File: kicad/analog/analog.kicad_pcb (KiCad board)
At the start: 2 copper layers, 75 x 50 mm, 62 parts, among them J301 CONN_02X05, Q201 DMG3414U, Q501 DMG3414U, Q601 DMG3414U, Q701 DMG3414U, U101 NCP694-3.3, U202 LTC2052, U301 SP3003-04, U401 REF5030, U402 LTC2052, U602 LTC2052

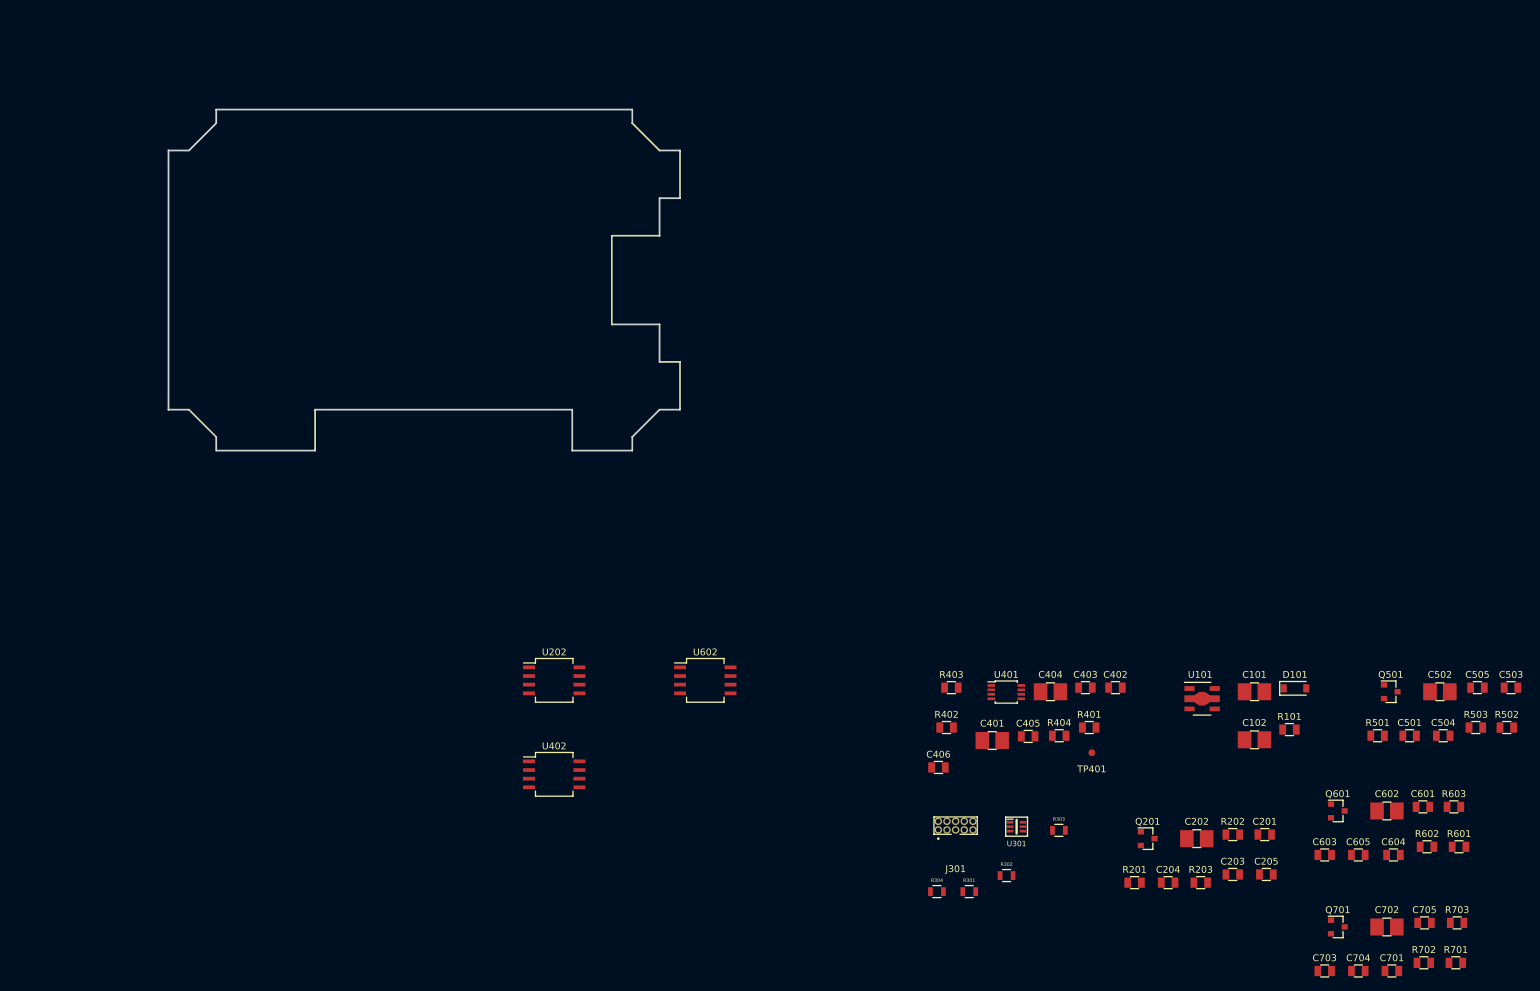
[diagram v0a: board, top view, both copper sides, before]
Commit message: Fix FCI connector refs, footprints, all packages for analog, starting parts placement
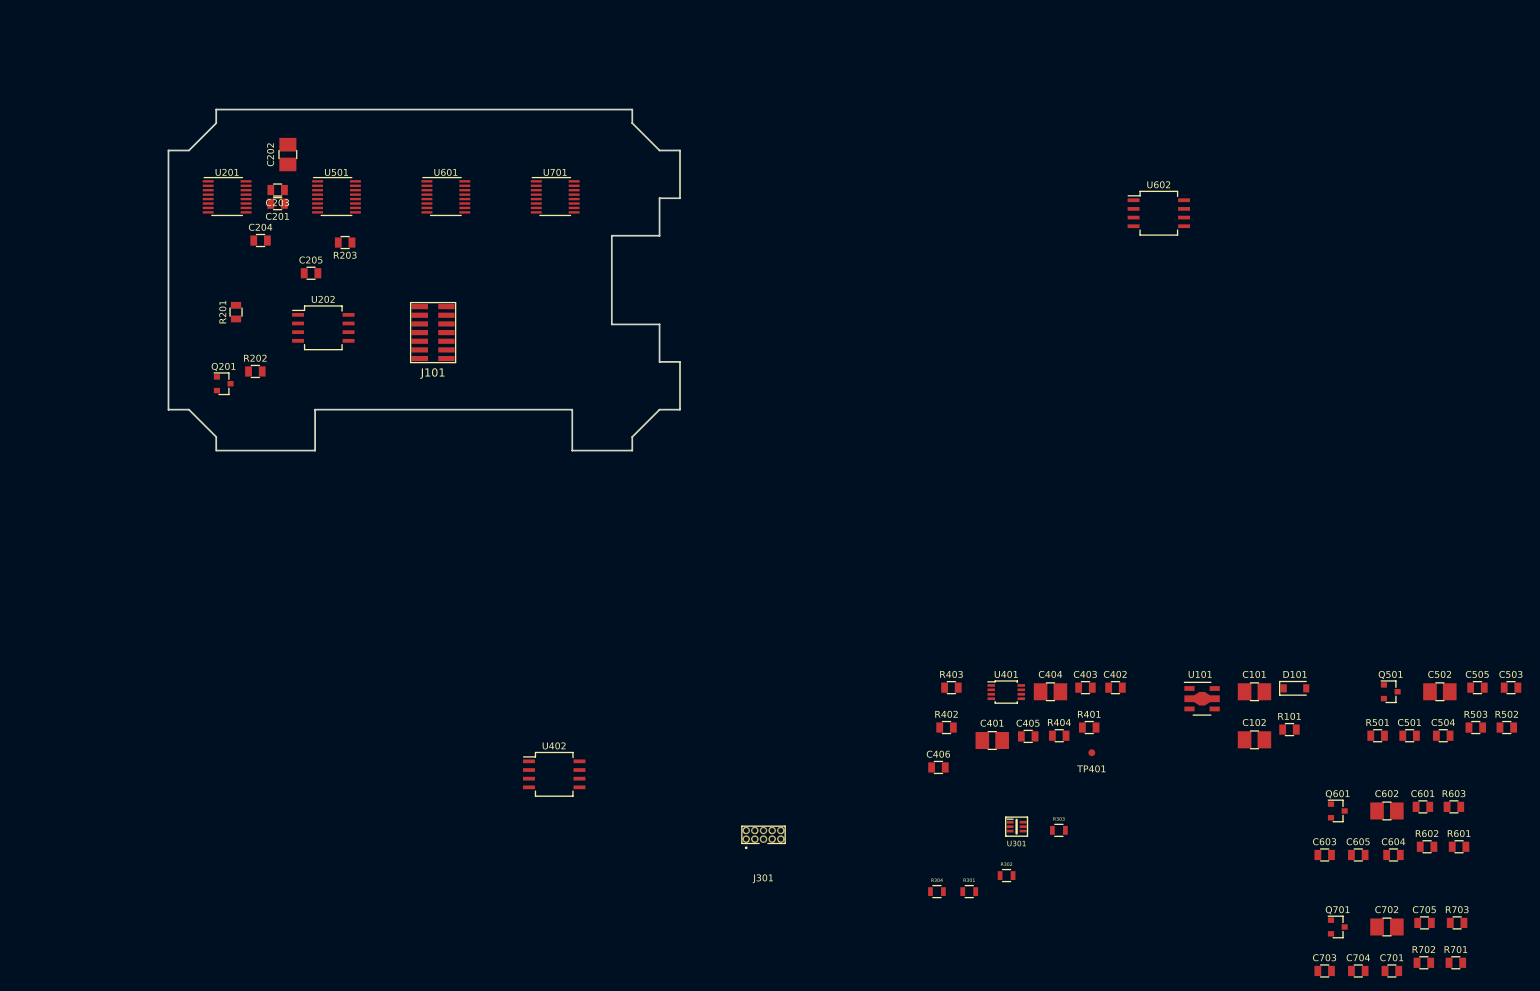
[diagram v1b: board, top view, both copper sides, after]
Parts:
- added J101: FCI 20021221-00014T4LF, paddle:conn_FCI_14_NH, F.Cu at (38.8, 32.7)
- added U201: ADS1220, paddle:TSSOP-16-1EP_4.4x5mm_Pitch0.65mm, F.Cu at (8.60, 12.8)
- added U501: ADS1220, paddle:TSSOP-16-1EP_4.4x5mm_Pitch0.65mm, F.Cu at (24.6, 12.8)
- added U601: ADS1220, paddle:TSSOP-16-1EP_4.4x5mm_Pitch0.65mm, F.Cu at (40.7, 12.8)
- added U701: ADS1220, paddle:TSSOP-16-1EP_4.4x5mm_Pitch0.65mm, F.Cu at (56.7, 12.8)
- moved C203 172.3 mm to (16.0, 11.8), turned to 180 degrees
- moved C201 171.8 mm to (16.0, 13.8), turned to 180 degrees
- moved C202 166.8 mm to (17.5, 6.60), turned to 90 degrees
- moved C205 165.5 mm to (20.9, 24.0)
- moved C204 163.0 mm to (13.5, 19.2)
- moved R202 158.6 mm to (12.7, 38.4)
- moved R203 156.7 mm to (25.9, 19.5), turned to 180 degrees
- moved R201 156.0 mm to (9.90, 29.7), turned to 90 degrees
- moved Q201 151.0 mm to (8.10, 40.2)
- moved U602 95.5 mm to (145.2, 15.2)
- moved U202 61.8 mm to (22.7, 32.0)
- moved J301 28.2 mm to (87.2, 106.3)
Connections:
- U301 pad 5: +3V3 -> +3.3VA
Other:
- copper layers 2 -> 4
- rule pad_to_mask_clearance: 0.2 -> 0.07

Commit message: separate opamps for - input
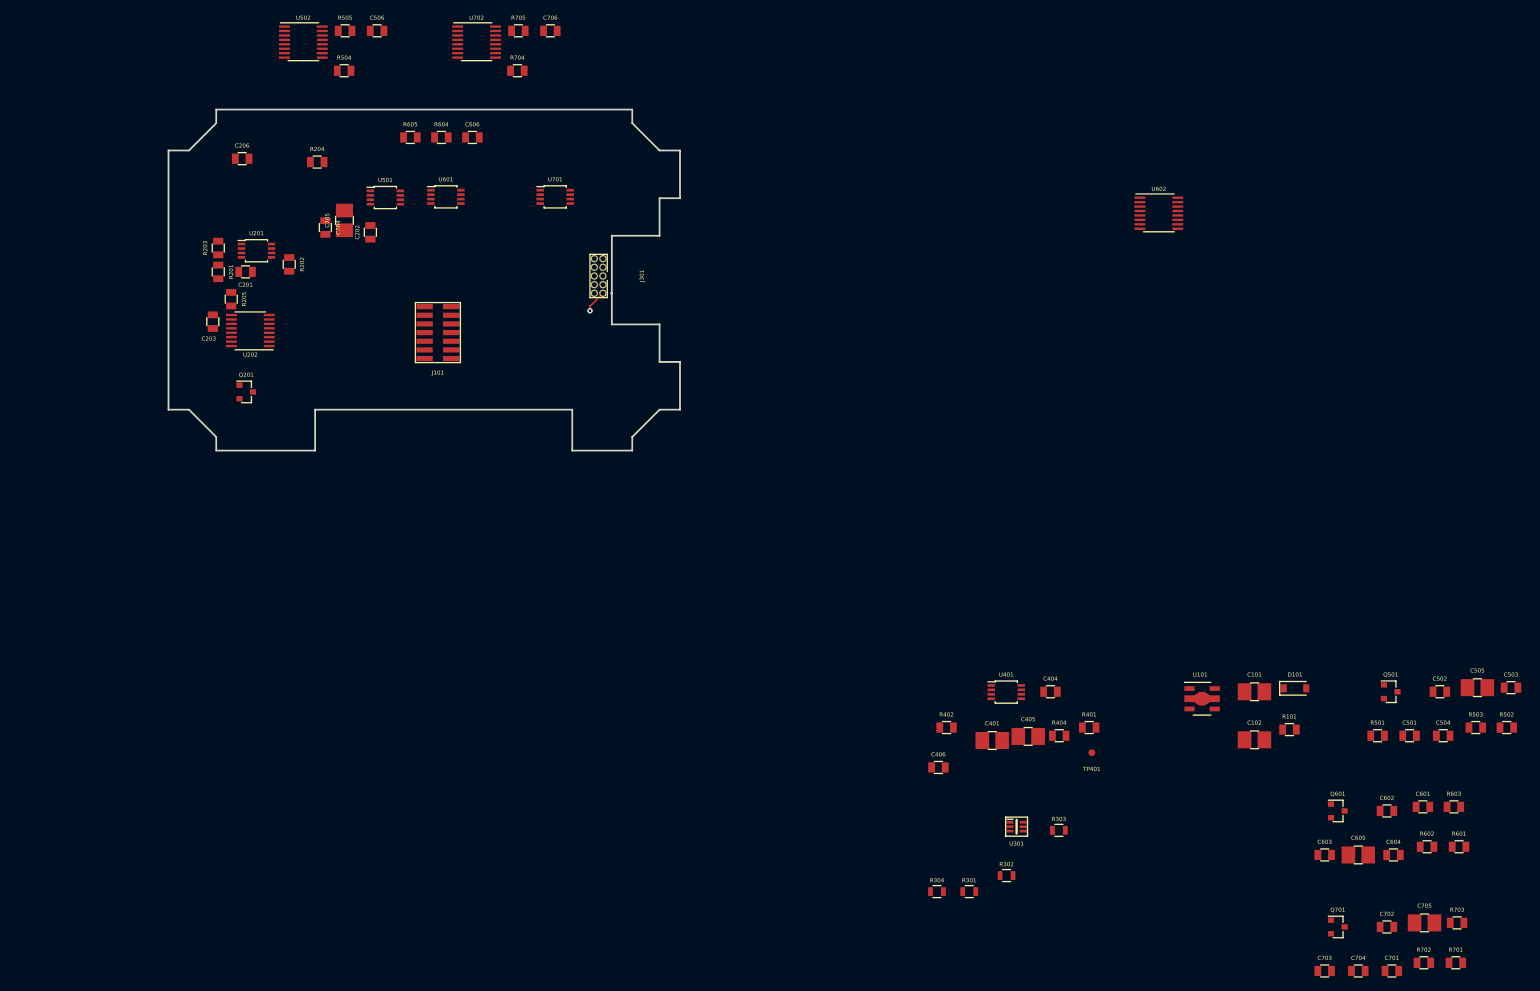
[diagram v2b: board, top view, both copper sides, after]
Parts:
- removed C402, C403: 1uF, paddle:SMD_0805
- removed R403: 20.0k 0.1%, paddle:SMD_0805
- removed U402: LTC2052, paddle:SO-8_5.3x6.2mm_Pitch1.27mm
- added C206: 0.1uF, paddle:SMD_0805, F.Cu at (10.8, 7.20)
- added C506: 0.1uF, paddle:SMD_0805, F.Cu at (30.6, -11.5)
- added C606: 0.1uF, paddle:SMD_0805, F.Cu at (44.6, 4.09)
- added C706: 0.1uF, paddle:SMD_0805, F.Cu at (56.0, -11.5)
- added R204: DNP, paddle:SMD_0805, F.Cu at (21.8, 7.70)
- added R205: 10.0k, paddle:SMD_0805, F.Cu at (9.20, 27.8)
- added R504: DNP, paddle:SMD_0805, F.Cu at (25.8, -5.69)
- added R505: 10.0k, paddle:SMD_0805, F.Cu at (25.9, -11.5)
- added R604: DNP, paddle:SMD_0805, F.Cu at (40.0, 4.09)
- added R605: 10.0k, paddle:SMD_0805, F.Cu at (35.5, 4.09)
- added R704: DNP, paddle:SMD_0805, F.Cu at (51.2, -5.69)
- added R705: 10.0k, paddle:SMD_0805, F.Cu at (51.3, -11.5)
- added U502: ADS1220, paddle:TSSOP-16-1EP_4.4x5mm_Pitch0.65mm, F.Cu at (19.8, -9.89)
- added U702: ADS1220, paddle:TSSOP-16-1EP_4.4x5mm_Pitch0.65mm, F.Cu at (45.2, -9.89)
- C201, C203, C501, C503, C601, C603, C701, C703: value 0.1uF -> 100pF
- C202, C502, C602, C702: value 10uF -> 100pF; footprint paddle:SMD_1206 -> paddle:SMD_0805
- C204, C504, C604, C704: value 100pF -> 0.1uF
- C205, C505, C605, C705: value 100pF -> 10uF; footprint paddle:SMD_0805 -> paddle:SMD_1206
- C404: value 10uF -> 1uF; footprint paddle:SMD_1206 -> paddle:SMD_0805
- C405: value 0.1uF -> 10uF; footprint paddle:SMD_0805 -> paddle:SMD_1206
- C406: value 100pF -> 1uF
- R202, R502, R602, R702: value 10.0k -> 20.0k
- R401: value 1R0 -> 20k 0.1%
- R402: value 20k 0.1% -> 20.0k 0.1%
- R404: value DNP -> 1R0
- U201, U501, U601, U701: value ADS1220 -> LTC2052; footprint paddle:TSSOP-16-1EP_4.4x5mm_Pitch0.65mm -> paddle:TSSOP-8_3x3mm_Pitch0.65mm
- U202, U602: value LTC2052 -> ADS1220; footprint paddle:SO-8_5.3x6.2mm_Pitch1.27mm -> paddle:TSSOP-16-1EP_4.4x5mm_Pitch0.65mm
- moved J301 85.4 mm to (63.1, 24.4), turned to 90 degrees
- moved C203 21.5 mm to (6.50, 31.1), turned to 270 degrees
- moved R203 18.6 mm to (7.30, 20.3), turned to 90 degrees
- moved C202 16.6 mm to (29.6, 18.0)
- moved R202 16.5 mm to (17.7, 22.7), turned to 270 degrees
- moved C201 11.0 mm to (11.3, 23.8)
- moved U202 10.7 mm to (12.0, 32.4), turned to 180 degrees
- moved C204 9.69 mm to (23.0, 17.3), turned to 270 degrees
- moved C205 9.17 mm to (25.8, 16.2), turned to 90 degrees
- moved U201 8.99 mm to (12.9, 20.7)
- moved U501 7.17 mm to (31.8, 12.9)
- moved R201 6.45 mm to (7.30, 23.8), turned to 270 degrees
- moved Q201 3.51 mm to (11.4, 41.4)
- moved J101 0.70 mm to (39.5, 32.7)
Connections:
- C201 pad 2: +3.3VA -> Net-(C201-Pad2)
- C202 pad 1: +3.3VA -> GND
- C202 pad 2: GND -> Net-(C202-Pad2)
- C203 pad 1: GND -> Net-(C203-Pad1)
- C203 pad 2: +3.3VA -> GND
- C204 pad 1: Net-(C204-Pad1) -> GND
- C204 pad 2: GND -> +3.3VA
- C205 pad 1: GND -> +3.3VA
- C205 pad 2: Net-(C205-Pad2) -> GND
- C405 pad 1: GND -> Net-(C405-Pad1)
- C405 pad 2: +3.3VA -> GND
- C406 pad 1: GND -> /VREF
- C406 pad 2: Net-(C406-Pad2) -> GND
- C501 pad 2: +3.3VA -> Net-(C501-Pad2)
- C502 pad 1: +3.3VA -> GND
- C502 pad 2: GND -> Net-(C502-Pad2)
- C503 pad 1: GND -> Net-(C503-Pad1)
- C503 pad 2: +3.3VA -> GND
- C504 pad 1: Net-(C504-Pad1) -> GND
- C504 pad 2: GND -> +3.3VA
- C505 pad 1: GND -> +3.3VA
- C505 pad 2: Net-(C505-Pad2) -> GND
- C601 pad 2: +3.3VA -> Net-(C601-Pad2)
- C602 pad 1: +3.3VA -> GND
- C602 pad 2: GND -> Net-(C602-Pad2)
- C603 pad 1: GND -> Net-(C603-Pad1)
- C603 pad 2: +3.3VA -> GND
- C604 pad 1: Net-(C604-Pad1) -> GND
- C604 pad 2: GND -> +3.3VA
- C605 pad 1: GND -> +3.3VA
- C605 pad 2: Net-(C605-Pad2) -> GND
- C701 pad 2: +3.3VA -> Net-(C701-Pad2)
- C702 pad 1: +3.3VA -> GND
- C702 pad 2: GND -> Net-(C702-Pad2)
- C703 pad 1: GND -> Net-(C703-Pad1)
- C703 pad 2: +3.3VA -> GND
- C704 pad 1: Net-(C704-Pad1) -> GND
- C704 pad 2: GND -> +3.3VA
- C705 pad 1: GND -> +3.3VA
- C705 pad 2: Net-(C705-Pad2) -> GND
- R201 pad 1: +3.3VA -> Net-(C201-Pad2)
- R201 pad 2: Net-(C204-Pad1) -> /IN_
- R202 pad 1: Net-(C205-Pad2) -> Net-(C202-Pad2)
- R202 pad 2: /IN_ -> /BRIDGE_COMP
- R203 pad 1: Net-(C205-Pad2) -> Net-(C201-Pad2)
- R401 pad 1: Net-(C404-Pad1) -> /BRIDGE_COMP
- R401 pad 2: /VREF -> +3.3VA
- R402 pad 1: Net-(C406-Pad2) -> GND
- R402 pad 2: +3.3VA -> /BRIDGE_COMP
- R404 pad 1: Net-(C406-Pad2) -> Net-(C405-Pad1)
- R404 pad 2: /BRIDGE_COMP -> /VREF
- R501 pad 1: +3.3VA -> Net-(C501-Pad2)
- R501 pad 2: Net-(C504-Pad1) -> /IN_
- R502 pad 1: Net-(C505-Pad2) -> Net-(C502-Pad2)
- R502 pad 2: /IN_ -> /BRIDGE_COMP
- R503 pad 1: Net-(C505-Pad2) -> Net-(C501-Pad2)
- R601 pad 1: +3.3VA -> Net-(C601-Pad2)
- R601 pad 2: Net-(C604-Pad1) -> /IN_
- R602 pad 1: Net-(C605-Pad2) -> Net-(C602-Pad2)
- R602 pad 2: /IN_ -> /BRIDGE_COMP
- R603 pad 1: Net-(C605-Pad2) -> Net-(C601-Pad2)
- R701 pad 1: +3.3VA -> Net-(C701-Pad2)
- R701 pad 2: Net-(C704-Pad1) -> /IN_
- R702 pad 1: Net-(C705-Pad2) -> Net-(C702-Pad2)
- R702 pad 2: /IN_ -> /BRIDGE_COMP
- R703 pad 1: Net-(C705-Pad2) -> Net-(C701-Pad2)
- U201 pad 1: /SPI_SCLK -> Net-(R203-Pad2)
- U201 pad 2: /AN0_CS* -> Net-(R203-Pad2)
- U201 pad 3: GND -> Net-(C201-Pad2)
- U201 pad 5: GND -> Net-(C202-Pad2)
- U201 pad 6: GND -> Net-(R204-Pad2)
- U201 pad 7: /BRIDGE_COMP -> Net-(R204-Pad2)
- U201 pad 8: GND -> +3.3VA
- U202 pad 1: Net-(R203-Pad2) -> /SPI_SCLK
- U202 pad 2: Net-(R203-Pad2) -> /AN0_CS*
- U202 pad 3: Net-(C205-Pad2) -> GND
- U202 pad 5: Net-(C505-Pad2) -> GND
- U202 pad 6: Net-(R503-Pad2) -> GND
- U202 pad 7: Net-(R503-Pad2) -> Net-(R204-Pad2)
- U202 pad 8: +3.3VA -> GND
- U401 pad 5: Net-(C403-Pad1) -> Net-(C404-Pad1)
- U501 pad 1: /SPI_SCLK -> Net-(R503-Pad2)
- U501 pad 2: /AN1_CS* -> Net-(R503-Pad2)
- U501 pad 3: GND -> Net-(C501-Pad2)
- U501 pad 5: GND -> Net-(C502-Pad2)
- U501 pad 6: GND -> Net-(R504-Pad2)
- U501 pad 7: /BRIDGE_COMP -> Net-(R504-Pad2)
- U501 pad 8: GND -> +3.3VA
- U601 pad 1: /SPI_SCLK -> Net-(R603-Pad2)
- U601 pad 2: /AN2_CS* -> Net-(R603-Pad2)
- U601 pad 3: GND -> Net-(C601-Pad2)
- U601 pad 5: GND -> Net-(C602-Pad2)
- U601 pad 6: GND -> Net-(R604-Pad2)
- U601 pad 7: /BRIDGE_COMP -> Net-(R604-Pad2)
- U601 pad 8: GND -> +3.3VA
- U602 pad 1: Net-(R603-Pad2) -> /SPI_SCLK
- U602 pad 2: Net-(R603-Pad2) -> /AN2_CS*
- U602 pad 3: Net-(C605-Pad2) -> GND
- U602 pad 5: Net-(C705-Pad2) -> GND
- U602 pad 6: Net-(R703-Pad2) -> GND
- U602 pad 7: Net-(R703-Pad2) -> Net-(R604-Pad2)
- U602 pad 8: +3.3VA -> GND
- U701 pad 1: /SPI_SCLK -> Net-(R703-Pad2)
- U701 pad 2: /AN3_CS* -> Net-(R703-Pad2)
- U701 pad 3: GND -> Net-(C701-Pad2)
- U701 pad 5: GND -> Net-(C702-Pad2)
- U701 pad 6: GND -> Net-(R704-Pad2)
- U701 pad 7: /BRIDGE_COMP -> Net-(R704-Pad2)
- U701 pad 8: GND -> +3.3VA
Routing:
- net +3.3VA: track 0.00 -> 3.91 mm, vias 0 -> 1
- added copper zone on In2.Cu, net +3.3VA
- added copper zone on In1.Cu, net GND

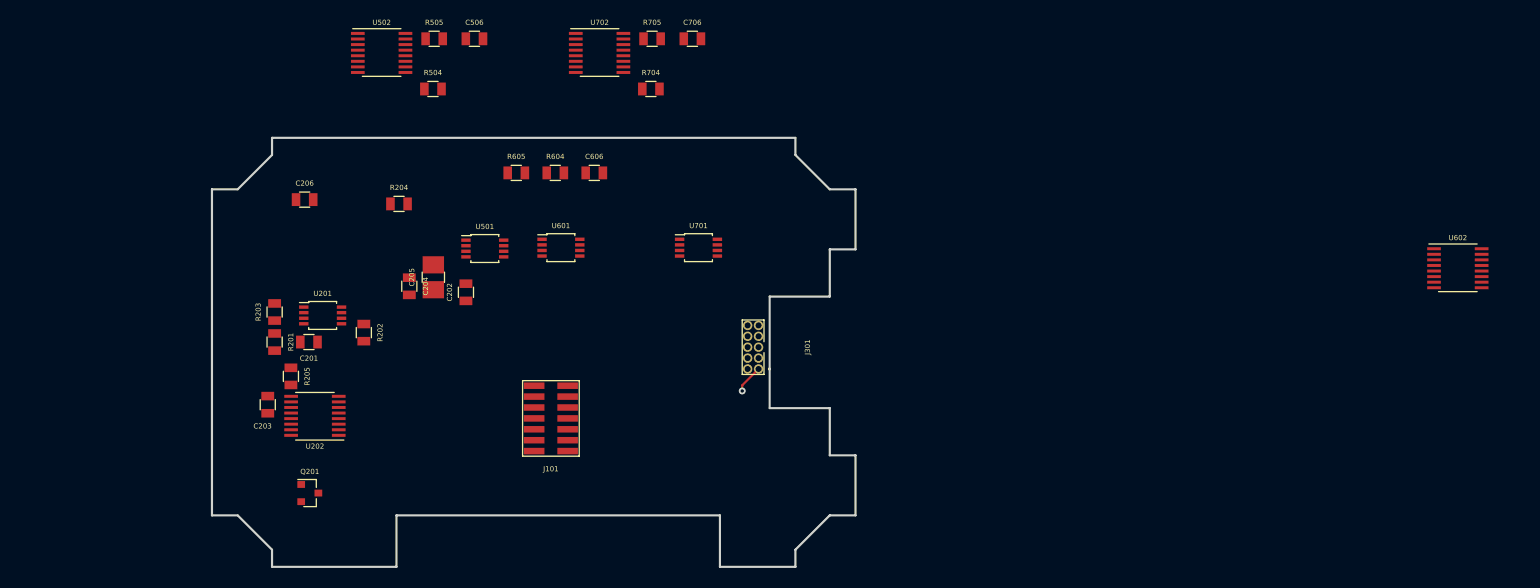
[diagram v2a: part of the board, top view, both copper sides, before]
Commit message: Sch: Added bypass caps opamps
Layout: placement and traces for 1 a/d channel ok, connector in right location and pinout (mirror image of processor)
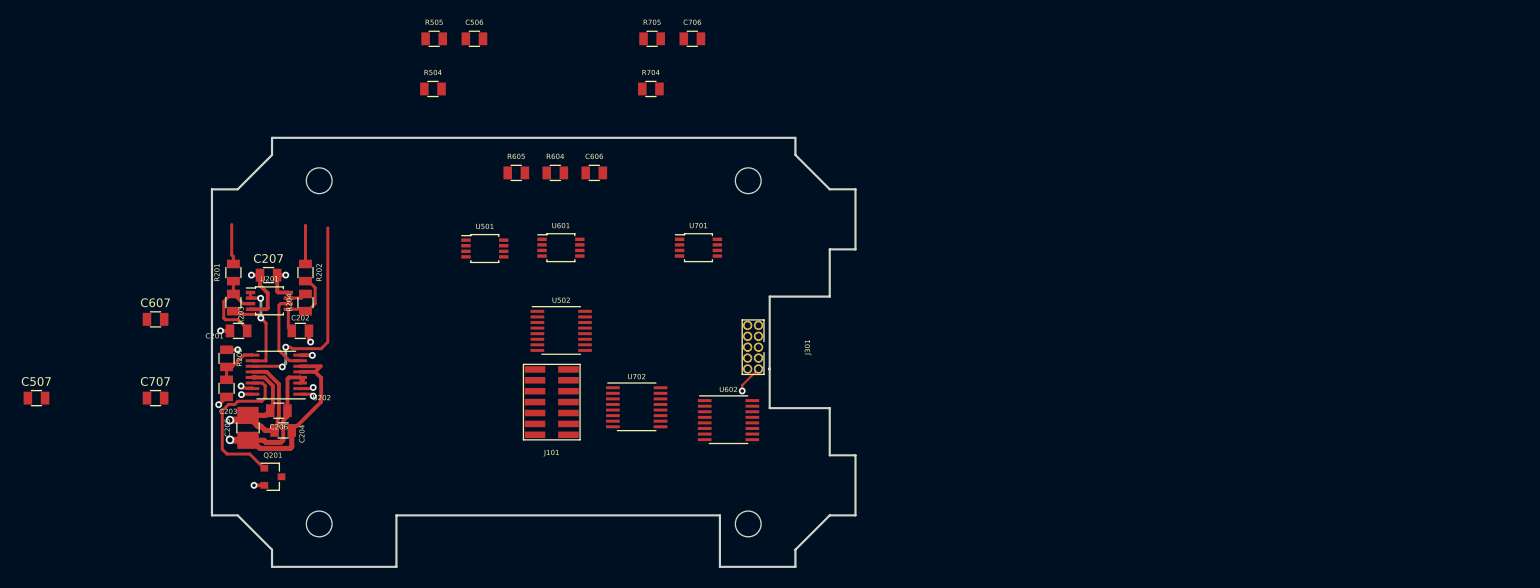
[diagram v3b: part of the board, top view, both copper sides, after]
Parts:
- added C207: 0.1uF, paddle:SMD_0805, F.Cu at (6.60, 16.0)
- added C507: 0.1uF, paddle:SMD_0805, F.Cu at (-20.5, 30.3)
- added C607: 0.1uF, paddle:SMD_0805, F.Cu at (-6.57, 21.2)
- added C707: 0.1uF, paddle:SMD_0805, F.Cu at (-6.57, 30.3)
- added REF**: hole, paddle:KH_F20_mounting_hole, F.Cu at (12.5, 45.0)
- added REF**: hole, paddle:KH_F20_mounting_hole, F.Cu at (62.5, 45.0)
- added REF**: hole, paddle:KH_F20_mounting_hole, F.Cu at (62.5, 5.00)
- added REF**: hole, paddle:KH_F20_mounting_hole, F.Cu at (12.5, 5.00)
- moved U602 86.8 mm to (60.2, 32.9)
- moved U702 41.5 mm to (49.5, 31.4)
- moved U502 38.6 mm to (40.7, 22.5)
- moved C205 27.8 mm to (4.20, 33.8), turned to 270 degrees
- moved C206 24.8 mm to (7.80, 31.8), turned to 180 degrees
- moved C204 22.3 mm to (8.30, 34.1), turned to 180 degrees
- moved C202 19.8 mm to (10.3, 22.5), turned to 180 degrees
- moved R204 15.8 mm to (10.9, 19.2), turned to 90 degrees
- moved R202 9.76 mm to (10.9, 15.7), turned to 90 degrees
- moved R201 9.42 mm to (2.50, 15.7), turned to 90 degrees
- moved C201 8.30 mm to (3.10, 22.5), turned to 0 degrees
- moved R205 7.79 mm to (1.70, 25.7)
- moved U202 6.58 mm to (7.50, 27.6)
- moved U201 6.43 mm to (6.70, 19.0)
- moved C203 5.16 mm to (1.70, 29.2)
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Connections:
- R201 pad 2: /IN_ -> /IN_0
- R501 pad 2: /IN_ -> /IN_1
- R601 pad 2: /IN_ -> /IN_2
- R701 pad 2: /IN_ -> /IN_3
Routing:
- net GND: track 0.00 -> 53.1 mm, vias 0 -> 7
- net +3.3VA: track 3.91 -> 34.5 mm, vias 1 -> 4
- net /VREF: track 0.00 -> 24.6 mm, vias 0 -> 2
- net Net-(Q201-Pad1): track 0.00 -> 18.9 mm
- net Net-(R203-Pad2): track 0.00 -> 14.6 mm, vias 0 -> 2
- net Net-(R204-Pad2): track 0.00 -> 12.2 mm
- net Net-(C201-Pad2): track 0.00 -> 11.1 mm
- net Net-(C202-Pad2): track 0.00 -> 9.61 mm
- net Net-(C203-Pad1): track 0.00 -> 5.12 mm
- net /IN_0: track 0.00 -> 4.68 mm
- net /BRIDGE_COMP: track 0.00 -> 4.50 mm
- net /SPI_SCLK: track 0.00 -> 1.62 mm, vias 0 -> 1
- net /AN0_CS*: track 0.00 -> 1.58 mm, vias 0 -> 1
- net /SPI_MISO: track 0.00 -> 1.46 mm, vias 0 -> 1
- net /SPI_MOSI: track 0.00 -> 1.31 mm, vias 0 -> 1
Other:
- net class Default: trace_width 0.25 -> 0.35
- net class PWR added: clearance 0.2, trace_width 0.45, via_dia 0.8, via_drill 0.4
